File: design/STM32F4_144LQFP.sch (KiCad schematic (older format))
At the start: 15 parts, among them P13 SWD, U4 STM32F40X_LQFP144, X2 8MHz 10ppm

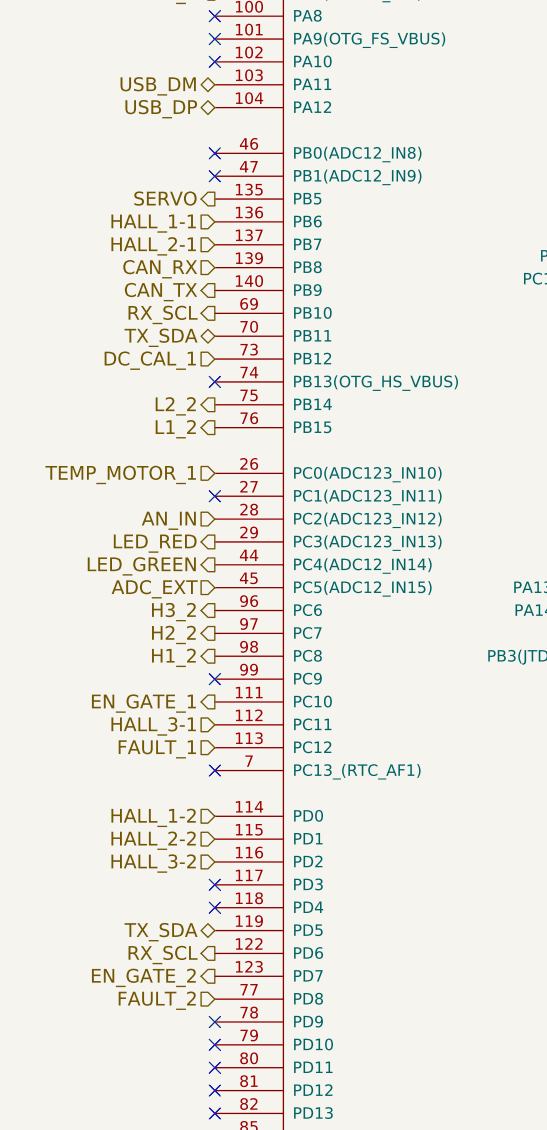
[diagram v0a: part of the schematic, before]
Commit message: Add pwr for second motor
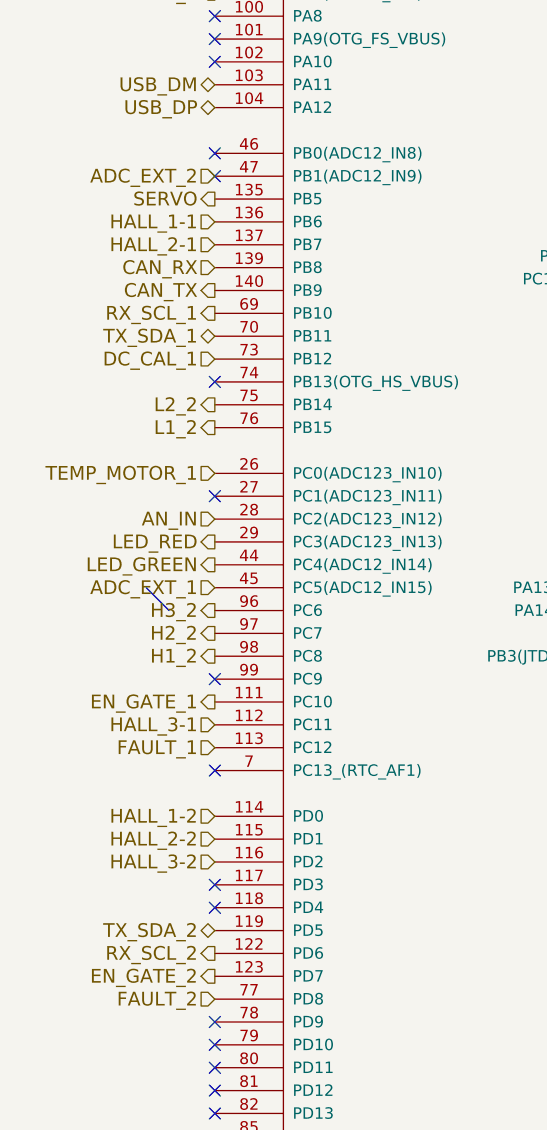
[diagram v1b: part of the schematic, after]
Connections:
- net labels added: ADC_EXT_1, ADC_EXT_2, RX_SCL_1, RX_SCL_2, TX_SDA_1, TX_SDA_2
- net labels removed: ADC_EXT, RX_SCL, TX_SDA
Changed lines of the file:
@@
 LIBS:crf_1
 LIBS:BLDC_4-cache
-EELAYER 27 0
+EELAYER 25 0
 EELAYER END
 $Descr A3 16535 11693
@@
 $EndComp
 $Comp
-L GND #PWR076
+L GND #PWR83
 U 1 1 53F757BC
 P 10250 9900
-F 0 "#PWR076" H 10250 9900 30  0001 C CNN
+F 0 "#PWR83" H 10250 9900 30  0001 C CNN
 F 1 "GND" H 10250 9830 30  0001 C CNN
 F 2 "" H 10250 9900 60  0001 C CNN
@@
 $EndComp
 $Comp
-L VCC #PWR077
+L VCC #PWR80
 U 1 1 53F757C2
 P 9650 8950
-F 0 "#PWR077" H 9650 9050 30  0001 C CNN
+F 0 "#PWR80" H 9650 9050 30  0001 C CNN
 F 1 "VCC" H 9650 9050 30  0000 C CNN
 F 2 "" H 9650 8950 60  0001 C CNN
@@
 $EndComp
 $Comp
-L GND #PWR078
+L GND #PWR78
 U 1 1 53F757C8
 P 9450 8500
-F 0 "#PWR078" H 9450 8500 30  0001 C CNN
+F 0 "#PWR78" H 9450 8500 30  0001 C CNN
 F 1 "GND" H 9450 8430 30  0001 C CNN
 F 2 "" H 9450 8500 60  0001 C CNN
@@
 $EndComp
 $Comp
-L VCC #PWR079
+L VCC #PWR77
 U 1 1 53F757CE
 P 9450 5300
-F 0 "#PWR079" H 9450 5400 30  0001 C CNN
+F 0 "#PWR77" H 9450 5400 30  0001 C CNN
 F 1 "VCC" H 9450 5400 30  0000 C CNN
 F 2 "" H 9450 5300 60  0001 C CNN
@@
 $EndComp
 $Comp
-L GND #PWR080
+L GND #PWR84
 U 1 1 53F757E9
 P 10500 2950
-F 0 "#PWR080" H 10500 2950 30  0001 C CNN
+F 0 "#PWR84" H 10500 2950 30  0001 C CNN
 F 1 "GND" H 10500 2880 30  0001 C CNN
 F 2 "" H 10500 2950 60  0001 C CNN
@@
 $EndComp
 $Comp
-L GND #PWR081
+L GND #PWR76
 U 1 1 53F757EF
 P 9400 3900
-F 0 "#PWR081" H 9400 3900 30  0001 C CNN
+F 0 "#PWR76" H 9400 3900 30  0001 C CNN
 F 1 "GND" H 9400 3830 30  0001 C CNN
 F 2 "" H 9400 3900 60  0001 C CNN
@@
 NoConn ~ 9250 3800
 $Comp
-L VCC #PWR082
+L VCC #PWR79
 U 1 1 53F75807
 P 9450 8700
-F 0 "#PWR082" H 9450 8800 30  0001 C CNN
+F 0 "#PWR79" H 9450 8800 30  0001 C CNN
 F 1 "VCC" H 9450 8800 30  0000 C CNN
 F 2 "" H 9450 8700 60  0001 C CNN
@@
 NoConn ~ 6950 4950
 $Comp
-L GND #PWR083
+L GND #PWR82
 U 1 1 53F75856
 P 10200 4650
-F 0 "#PWR083" H 10200 4650 30  0001 C CNN
+F 0 "#PWR82" H 10200 4650 30  0001 C CNN
 F 1 "GND" H 10200 4580 30  0001 C CNN
 F 2 "" H 10200 4650 60  0001 C CNN
@@
 $EndComp
 $Comp
-L VCC #PWR084
+L VCC #PWR88
 U 1 1 53F77417
 P 14000 4650
-F 0 "#PWR084" H 14000 4750 30  0001 C CNN
+F 0 "#PWR88" H 14000 4750 30  0001 C CNN
 F 1 "VCC" H 14000 4750 30  0000 C CNN
 F 2 "" H 14000 4650 60  0001 C CNN
@@
 $EndComp
 $Comp
-L GND #PWR085
+L GND #PWR87
 U 1 1 53F7741D
 P 13700 5000
-F 0 "#PWR085" H 13700 5000 30  0001 C CNN
+F 0 "#PWR87" H 13700 5000 30  0001 C CNN
 F 1 "GND" H 13700 4930 30  0001 C CNN
 F 2 "" H 13700 5000 60  0001 C CNN
@@
 $EndComp
 $Comp
-L GND #PWR086
+L GND #PWR86
 U 1 1 53F7743B
 P 13200 3550
-F 0 "#PWR086" H 13200 3550 30  0001 C CNN
+F 0 "#PWR86" H 13200 3550 30  0001 C CNN
 F 1 "GND" H 13200 3480 30  0001 C CNN
 F 2 "" H 13200 3550 60  0001 C CNN
@@
 $EndComp
 $Comp
-L VCC #PWR087
+L VCC #PWR85
 U 1 1 53F77441
 P 13200 2850
-F 0 "#PWR087" H 13200 2950 30  0001 C CNN
+F 0 "#PWR85" H 13200 2950 30  0001 C CNN
 F 1 "VCC" H 13200 2950 30  0000 C CNN
 F 2 "" H 13200 2850 60  0001 C CNN
@@
 HALL_3-2
 Text HLabel 6950 3350 0    60   Output ~ 0
-RX_SCL
+RX_SCL_1
 Text HLabel 6950 3450 0    60   3State ~ 0
-TX_SDA
+TX_SDA_1
 Text HLabel 6950 4050 0    60   Input ~ 0
 TEMP_MOTOR_1
@@
 L1_1
 Text HLabel 6950 4550 0    60   Input ~ 0
-ADC_EXT
+ADC_EXT_1
 Text HLabel 6950 6050 0    60   3State ~ 0
-TX_SDA
+TX_SDA_2
 Text HLabel 6950 6150 0    60   Output ~ 0
-RX_SCL
+RX_SCL_2
 Text HLabel 6950 5250 0    60   Input ~ 0
 FAULT_1
@@
 9D 20 C6 37 81 40 20 10 08 04 02 81 D0 4E 10 E3 9B 40 20 10 08 04 02 81 40 68 27 88 F1 4D 20 10
 08 04 02 81 40 20 B4 13 C4 F8 26 10 08 04 02 81 40 20 10 DA 89 FF 07 6E 76 4C 5E B7 9B F3 6C 00
-00 00 00 49 45 4E 44 AE 42 60 82 0A $EndBitmap
+00 00 00 49 45 4E 44 AE 42 60 82 09
 EndData
 $EndBitmap
@@
 $EndComp
 $Comp
-L GND #PWR088
+L GND #PWR81
 U 1 1 54097D19
 P 10000 3500
-F 0 "#PWR088" H 10000 3500 30  0001 C CNN
+F 0 "#PWR81" H 10000 3500 30  0001 C CNN
 F 1 "GND" H 10000 3430 30  0001 C CNN
 F 2 "" H 10000 3500 60  0001 C CNN
@@
 24 B8 E9 E2 F8 3F 8D 33 37 B1 3E 08 A4 52 29 90 67 22 91 08 C2 CB 20 79 AB AA AA 8A C3 E1 40 3D
 34 A5 52 09 D5 98 B2 D9 2C BE D6 C5 81 E3 5A E2 AA 04 42 E2 C0 81 E3 9D F0 FF 00 C6 F3 18 06 A9
-54 32 E1 00 00 00 00 49 45 4E 44 AE 42 60 82 00 $EndBitmap
+54 32 E1 00 00 00 00 49 45 4E 44 AE 42 60 82 00
 EndData
 $EndBitmap
@@
 NoConn ~ 9250 2750
 NoConn ~ 9250 2650
+Text HLabel 6950 2750 0    60   Input ~ 0
+ADC_EXT_2
+Entry Bus Bus
+	6650 4550 6750 4650
 $EndSCHEMATC

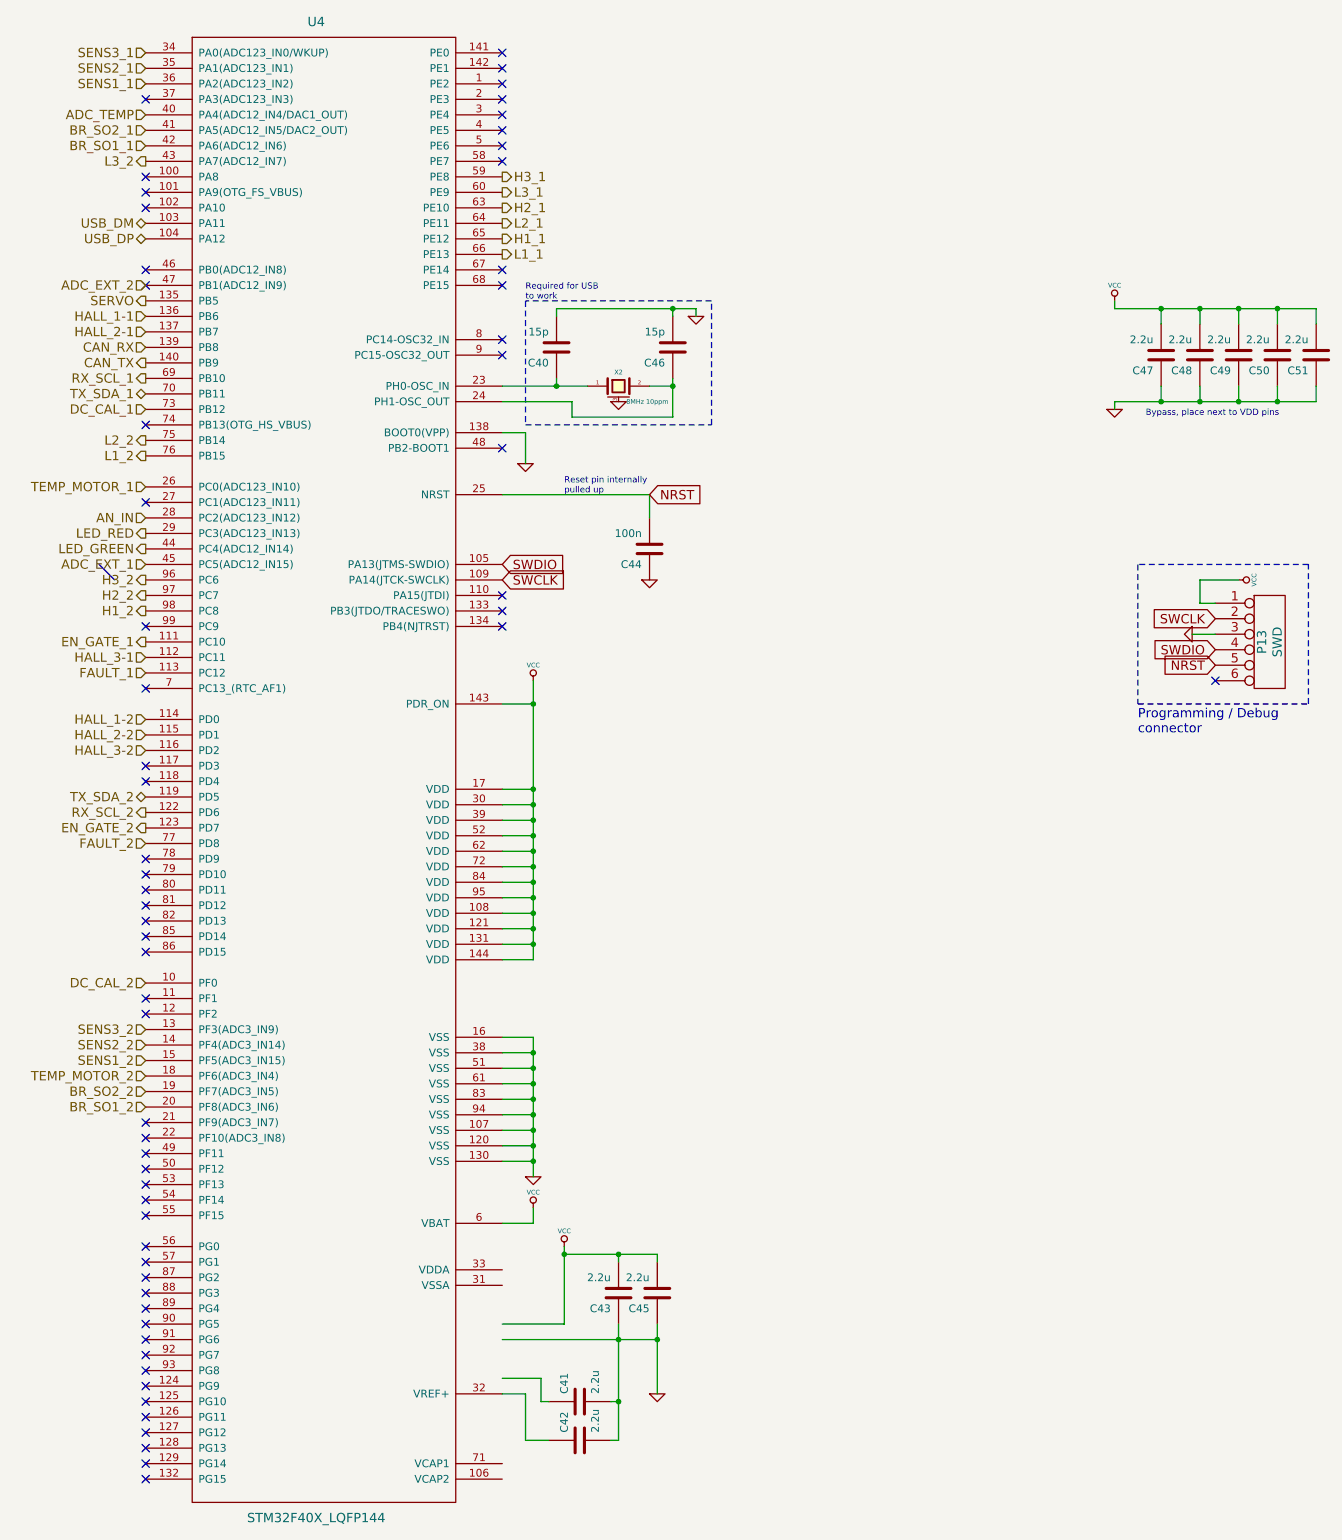
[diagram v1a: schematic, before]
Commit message: Fix some ERC error, add decoupling cap to Vref+ and make some small changes to lib
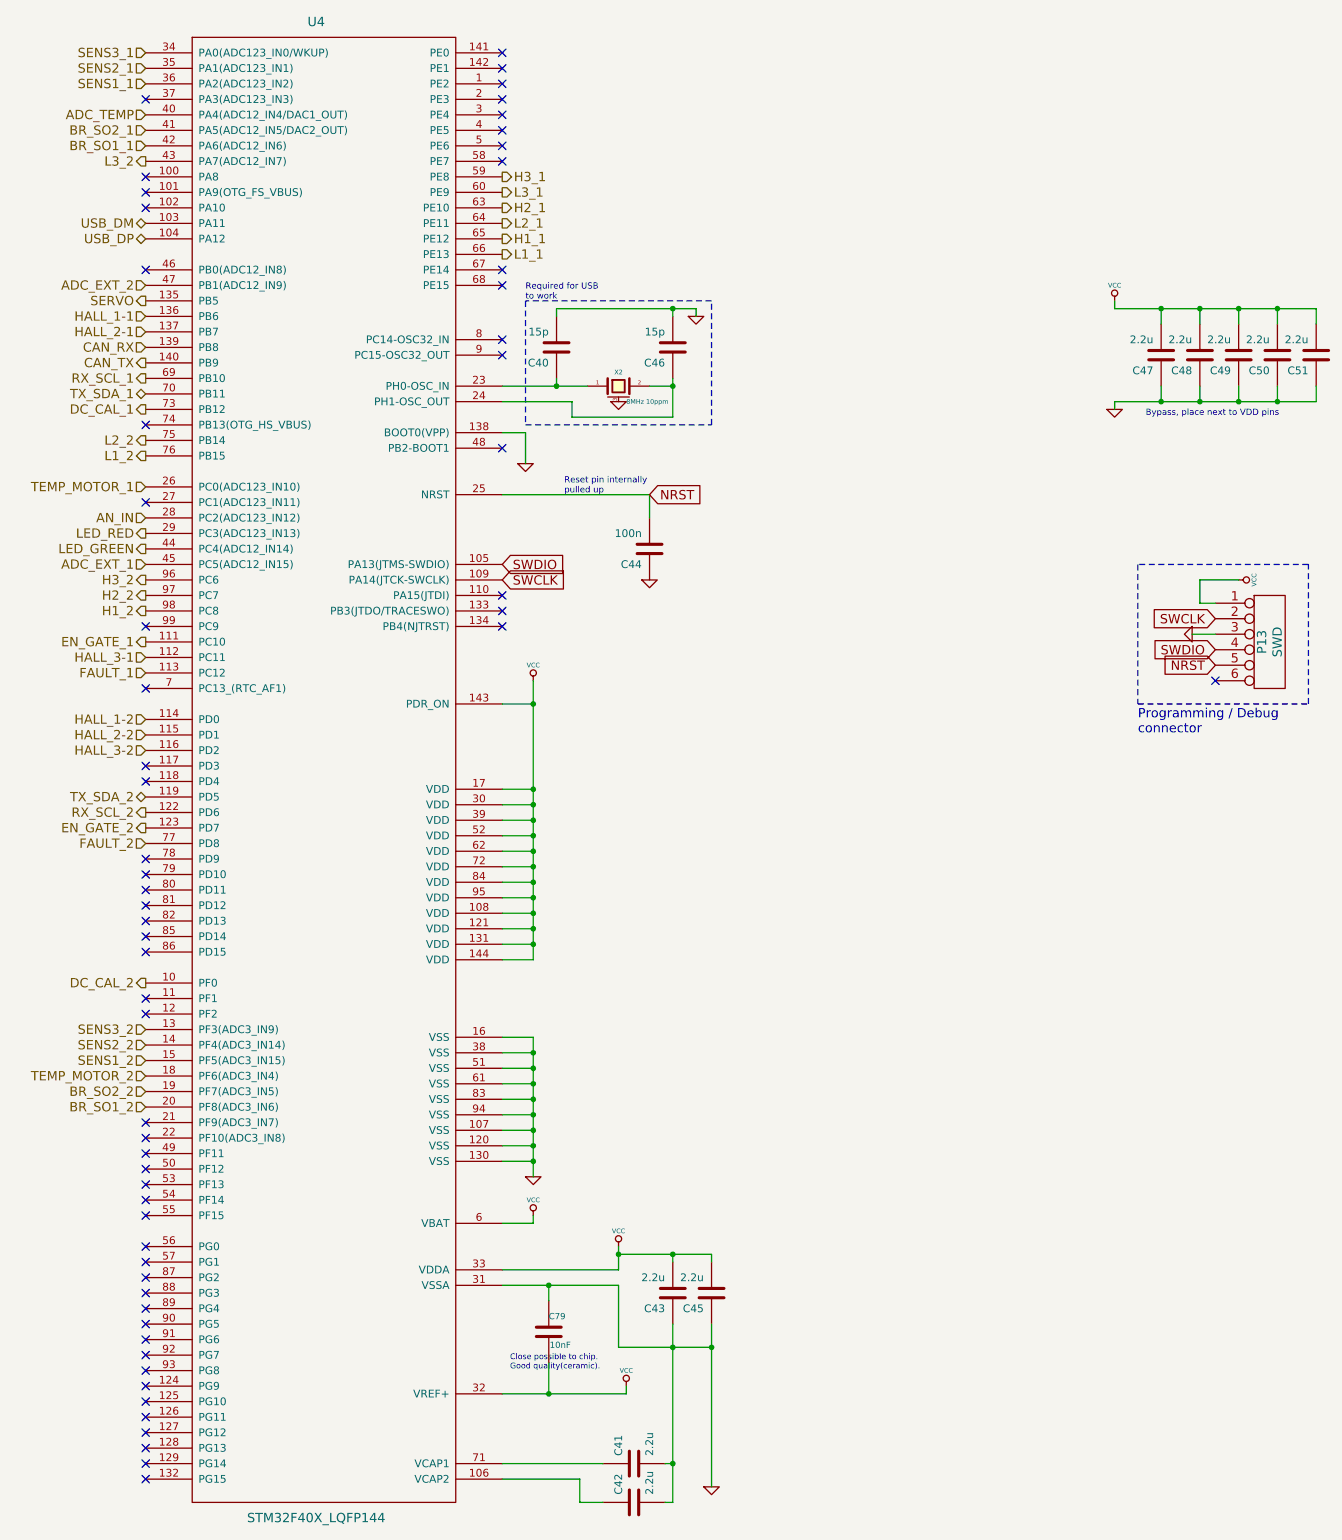
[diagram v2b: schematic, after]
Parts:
- added C79: 10nF, symbol C
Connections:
- wire segments 76 -> 80
- no-connect marks 61 -> 60
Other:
- note added: "Close possible to chip.\nGood quality(ceramic)."
- moved on the sheet: C41, C42, C43, C45

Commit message: Chnge name of crf lib and add footprint for new cap
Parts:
- C79: footprint (none) -> SMD_Packages:SMD-0603_c
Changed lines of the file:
@@
 9D 20 C6 37 81 40 20 10 08 04 02 81 D0 4E 10 E3 9B 40 20 10 08 04 02 81 40 68 27 88 F1 4D 20 10
 08 04 02 81 40 20 B4 13 C4 F8 26 10 08 04 02 81 40 20 10 DA 89 FF 07 6E 76 4C 5E B7 9B F3 6C 00
-00 00 00 49 45 4E 44 AE 42 60 82 0B
+00 00 00 49 45 4E 44 AE 42 60 82 0C
 EndData
 $EndBitmap
@@
 F 0 "C79" H 9550 9600 40  0000 L CNN
 F 1 "10nF" H 9556 9415 40  0000 L CNN
-F 2 "" H 9588 9350 30  0000 C CNN
+F 2 "SMD_Packages:SMD-0603_c" H 9588 9350 30  0001 C CNN
 F 3 "" H 9550 9500 60  0000 C CNN
 	1    9550 9500

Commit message: Some fixes in libs,schemas and netlist. Start new PCB
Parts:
- U4: footprint ~ -> Housings_QFP:TQFP-144_20x20mm_Pitch0.5mm
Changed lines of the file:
@@
 F 0 "U4" H 8050 7250 60  0000 C CNN
 F 1 "STM32F40X_LQFP144" H 8050 -2400 60  0000 C CNN
-F 2 "~" H 8100 4150 60  0000 C CNN
+F 2 "Housings_QFP:TQFP-144_20x20mm_Pitch0.5mm" H 8100 4150 60  0001 C CNN
 F 3 "~" H 8100 4150 60  0000 C CNN
 	1    8100 4150
